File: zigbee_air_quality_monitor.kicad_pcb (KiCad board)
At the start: 4 copper layers, 19.8 x 50.9 mm, 38 parts, among them J1 USB_C_Receptacle_USB2.0, J2 QWIIC, J3 Conn_02x02_Odd_Even, SW1 PAIR_BTN, SW2 USER_BTN, U1 USBLC6-2SC6, U2 BT840, U3 XC6206P332MR, U4 SCD40-D-R2, U6 TXS0102DCU

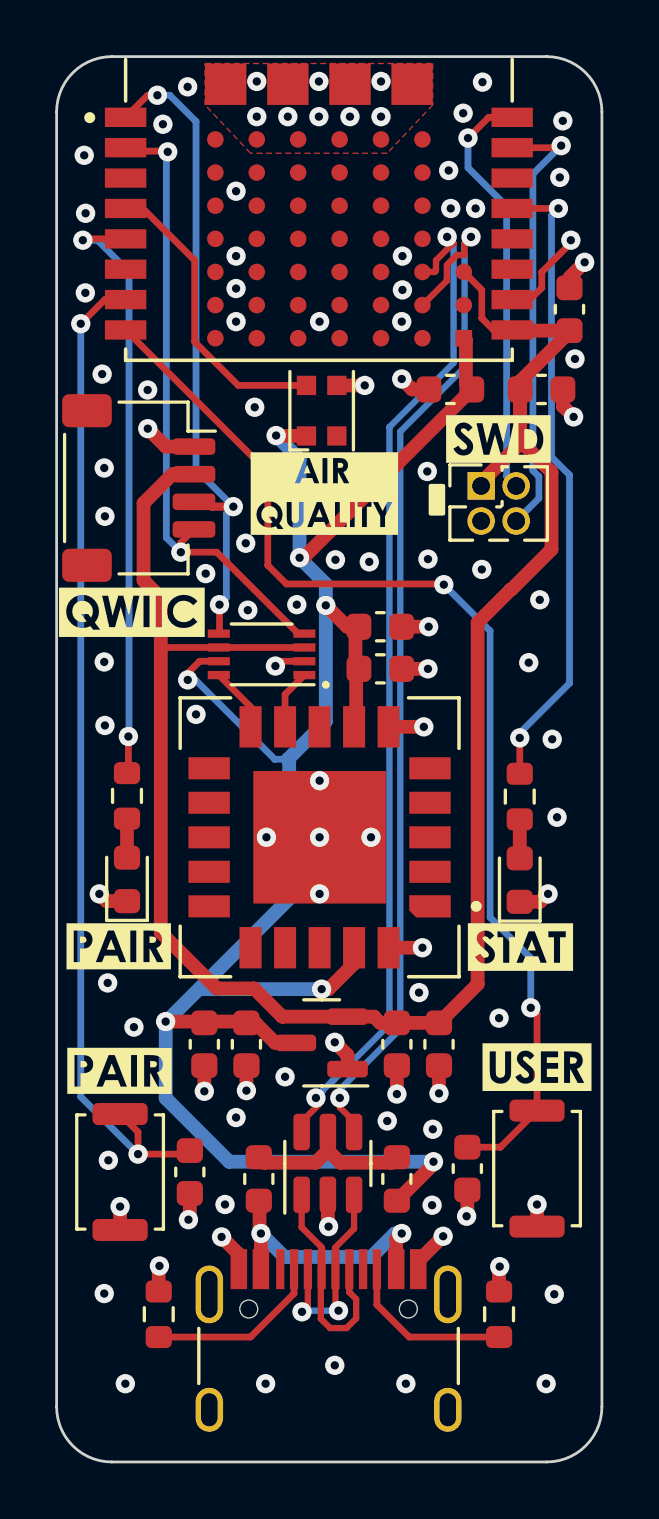
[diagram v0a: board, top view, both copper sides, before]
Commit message: rev2
Fixed RGB LED footprint, removed problematic button caps, cleaning
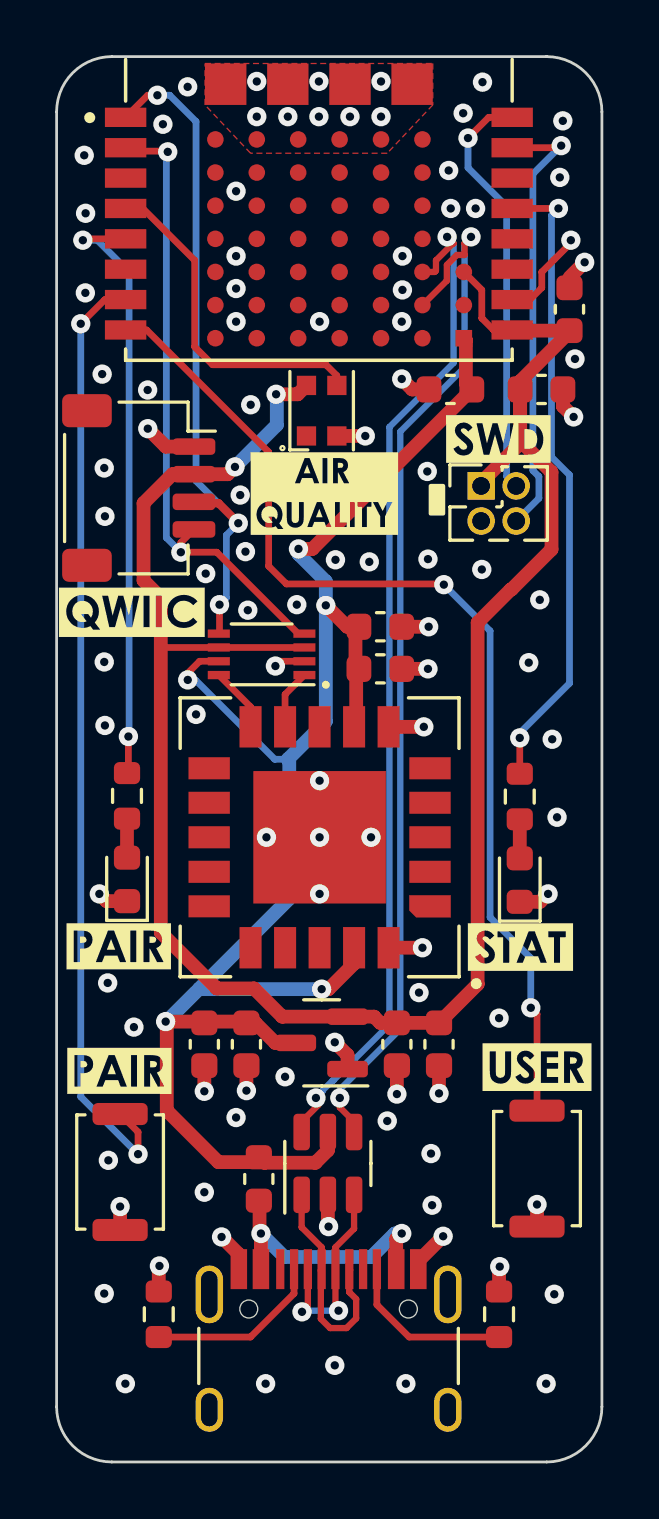
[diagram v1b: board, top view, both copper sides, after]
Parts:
- removed C1, C2: 100nF, Capacitor_SMD:C_0603_1608Metric
- removed FB1: 100R, Inductor_SMD:L_0603_1608Metric
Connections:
- C10 pad 1: VCC -> VBUS
- C11 pad 1: VCC -> VBUS
- C3 pad 1: VCC -> VBUS
- C5 pad 1: VCC -> VBUS
- C7 pad 1: VCC -> VBUS
- D3 pad 1: VCC -> unconnected-(D3-DOUT-Pad1)
- D3 pad 2: unconnected-(D3-DOUT-Pad2) -> GND
- D3 pad 3: GND -> /AIR_QUALITY_LED
- D3 pad 4: /AIR_QUALITY_LED -> +3.3V
- J1 pad S1: (no net) -> unconnected-(J1-SHIELD-PadS1)_1
- U2 pad F6: VCC -> VBUS
- U3 pad 3: VCC -> VBUS
- U4 pad 19: VCC -> VBUS
- U4 pad 7: VCC -> VBUS
- U6 pad 7: VCC -> VBUS
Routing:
- net VCC: track 75.0 -> 0.00 mm, vias 7 -> 0
- net VBUS: track 6.20 -> 64.8 mm, vias 0 -> 5
- net +3.3V: track 72.1 -> 78.2 mm, vias 0 -> 2
- net /USER_BTN: track 40.8 -> 38.2 mm
- net /PAIR_BTN: track 36.6 -> 34.6 mm
- net GND: track 32.2 -> 30.3 mm, vias 100 -> 99
- net /AIR_QUALITY_LED: track 10.9 -> 12.3 mm
- net /I2C_SDA_3V3: track 23.7 -> 24.2 mm
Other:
- board text added: "Jan Gnip rev2 08/24"
- board text removed: "Jan Gnip rev1 03/24"

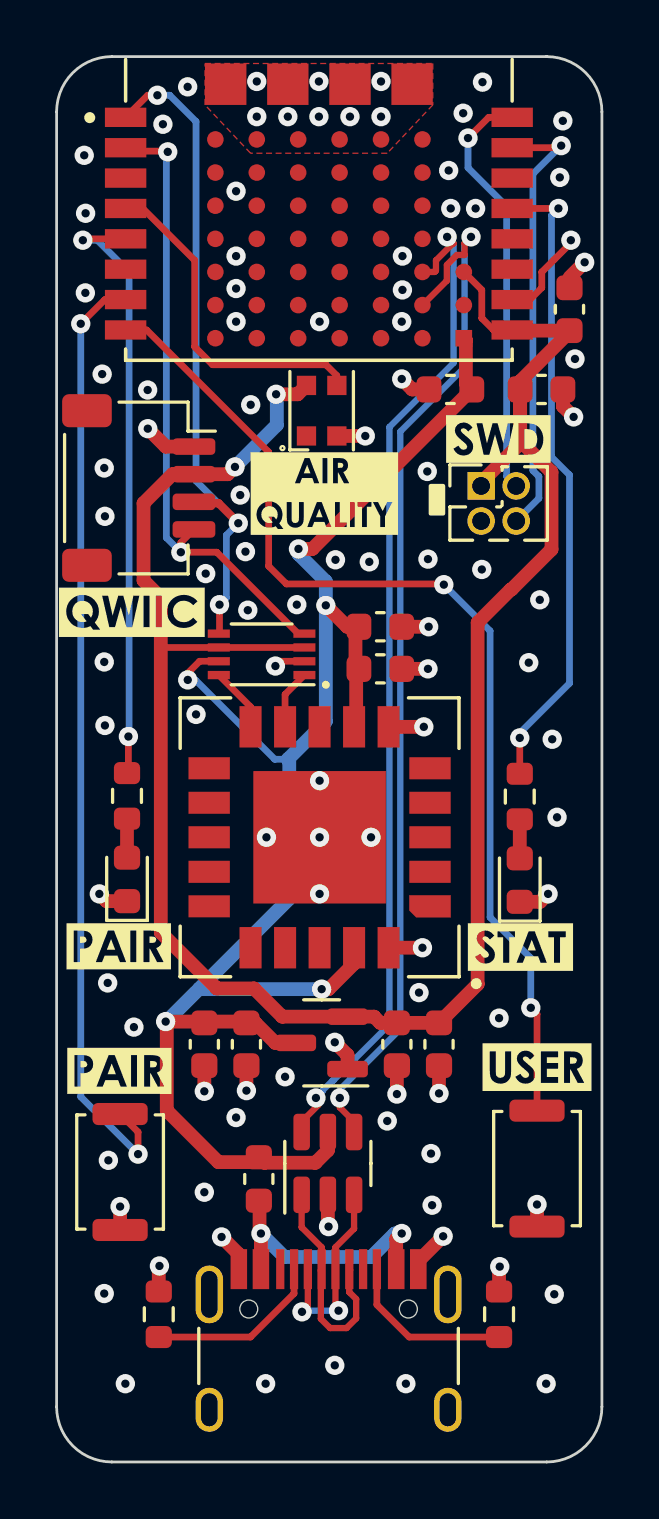
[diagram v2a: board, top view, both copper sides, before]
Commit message: Buttons aligned
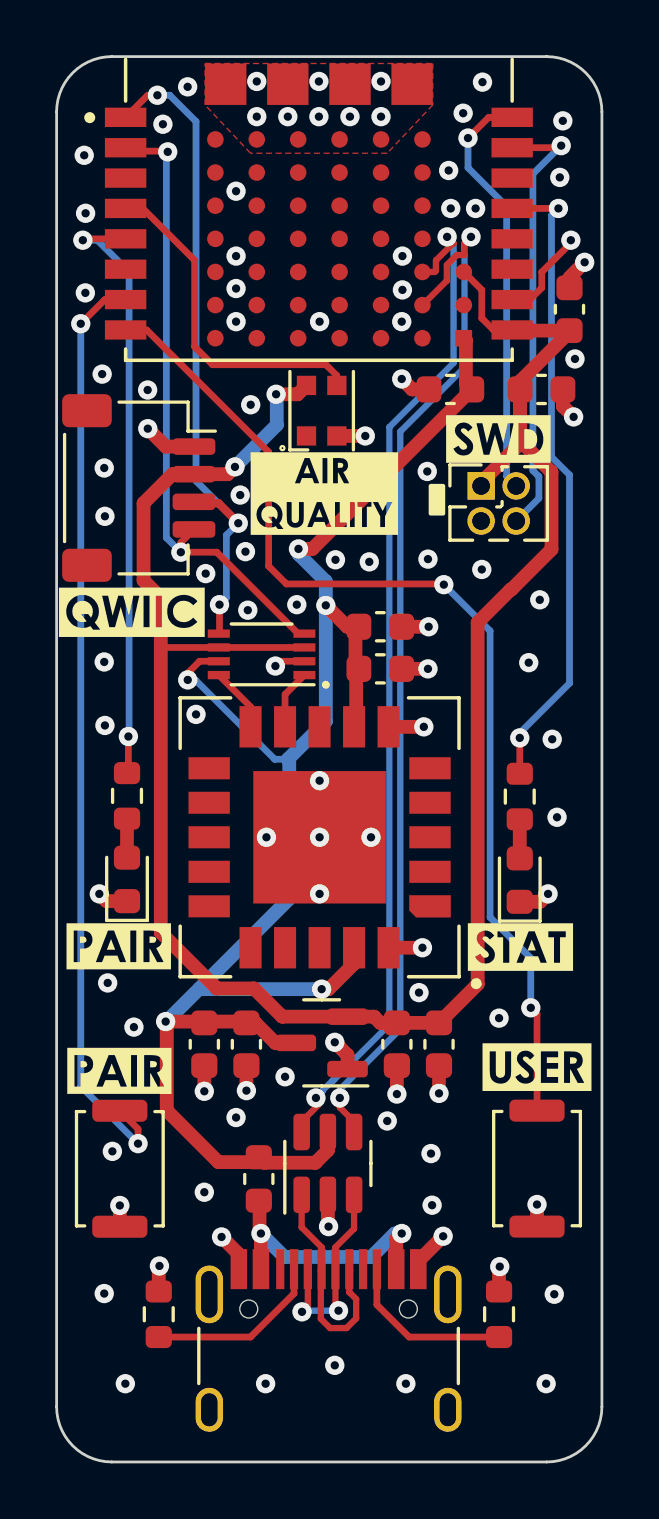
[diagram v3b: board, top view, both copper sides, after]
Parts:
- moved SW1 0.12 mm to (124.4, 129.5)
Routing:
- net /PAIR_BTN: track 34.6 -> 34.0 mm
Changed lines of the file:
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@@
 	(footprint "Button_Switch_SMD:SW_Push_SPST_NO_Alps_SKRK"
 		(layer "F.Cu")
-		(at 124.4 129.597694 -90)
+		(at 124.39 129.48 -90)
 		(descr "http://www.alps.com/prod/info/E/HTML/Tact/SurfaceMount/SKRK/SKRKAHE020.html")
 		(tags "SMD SMT button")
@@
 	)
 	(segment
+		(start 124.39 130.81)
+		(end 124.39 131.58)
+		(width 0.5)
+		(layer "F.Cu")
+		(net 1)
+	)
+	(segment
 		(start 139.245 98)
 		(end 139.6725 97.5725)
@@
 	)
 	(segment
-		(start 124.4 131.697694)
-		(end 124.4 130.85)
-		(width 0.5)
-		(layer "F.Cu")
-		(net 1)
-	)
-	(segment
 		(start 139.5 131.575)
 		(end 139.5 130.775)
@@
 	)
 	(via
-		(at 124.4 130.85)
+		(at 124.39 130.81)
 		(size 0.7)
 		(drill 0.3)
@@
 	)
 	(via
-		(at 123.975 129.175)
+		(at 124.12 128.85)
 		(size 0.7)
 		(drill 0.3)
@@
 	)
 	(segment
-		(start 125.05 128.147694)
-		(end 125.05 128.95)
+		(start 124.6 98)
+		(end 123.85 98)
 		(width 0.245)
 		(layer "F.Cu")
@@
 	)
 	(segment
-		(start 124.6 98)
-		(end 123.85 98)
+		(start 125.05 128.57)
+		(end 125.05 128.04)
 		(width 0.245)
 		(layer "F.Cu")
@@
 	)
 	(segment
-		(start 124.4 127.497694)
-		(end 125.05 128.147694)
+		(start 125.05 128.04)
+		(end 124.39 127.38)
 		(width 0.245)
 		(layer "F.Cu")
@@
 	)
 	(via
-		(at 125.05 128.95)
+		(at 125.05 128.57)
 		(size 0.7)
 		(drill 0.3)
@@
 	)
 	(segment
-		(start 122.975 98.875)
-		(end 122.975 126.875)
+		(start 125.05 128.57)
+		(end 122.975 126.495)
 		(width 0.245)
 		(layer "B.Cu")
@@
 	)
 	(segment
-		(start 122.975 126.875)
-		(end 125.05 128.95)
+		(start 122.975 126.495)
+		(end 122.975 98.875)
 		(width 0.245)
 		(layer "B.Cu")
@@
 	)
 	(group ""
-		(members "7d71db0d-f3d1-452f-9c5a-29f158d9e972" "c4e618ff-9b52-4491-9bb7-bafbd50dbeb6")
-	)
-	(group ""
